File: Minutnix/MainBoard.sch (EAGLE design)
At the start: 142 parts, among them IC1 MEGA8-AI, IC10 TPIC6C596PW, IC11 TPIC6C596PW, IC12 TPIC6C596PW, IC13 TPIC6C596PW, IC2 TPIC6C596PW, IC3 TPIC6C596PW, IC4 TPIC6C596PW, IC5 TPIC6C596PW, IC6 TP4056, IC7 FT232RL, IC9 SC4503, Q4 32.768kHz, T1 DMN3024LSD, X1 FH12-12S-0.5SH, X2 87438-03, X3 87438-03

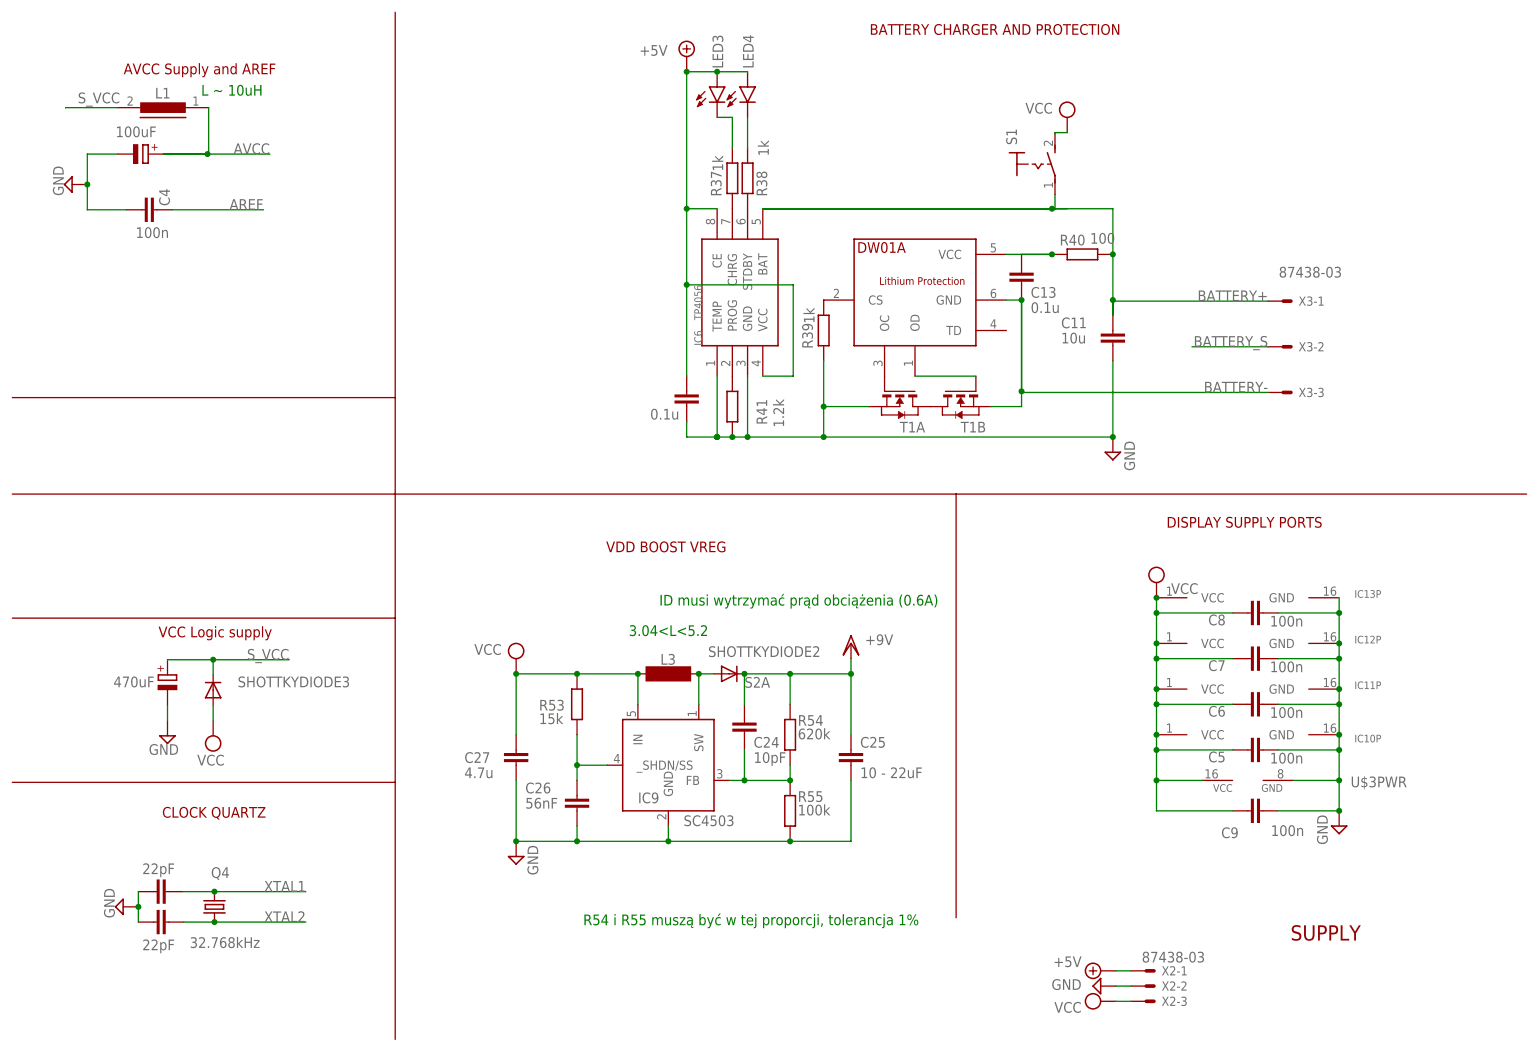
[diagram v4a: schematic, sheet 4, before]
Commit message: new lib + board progress
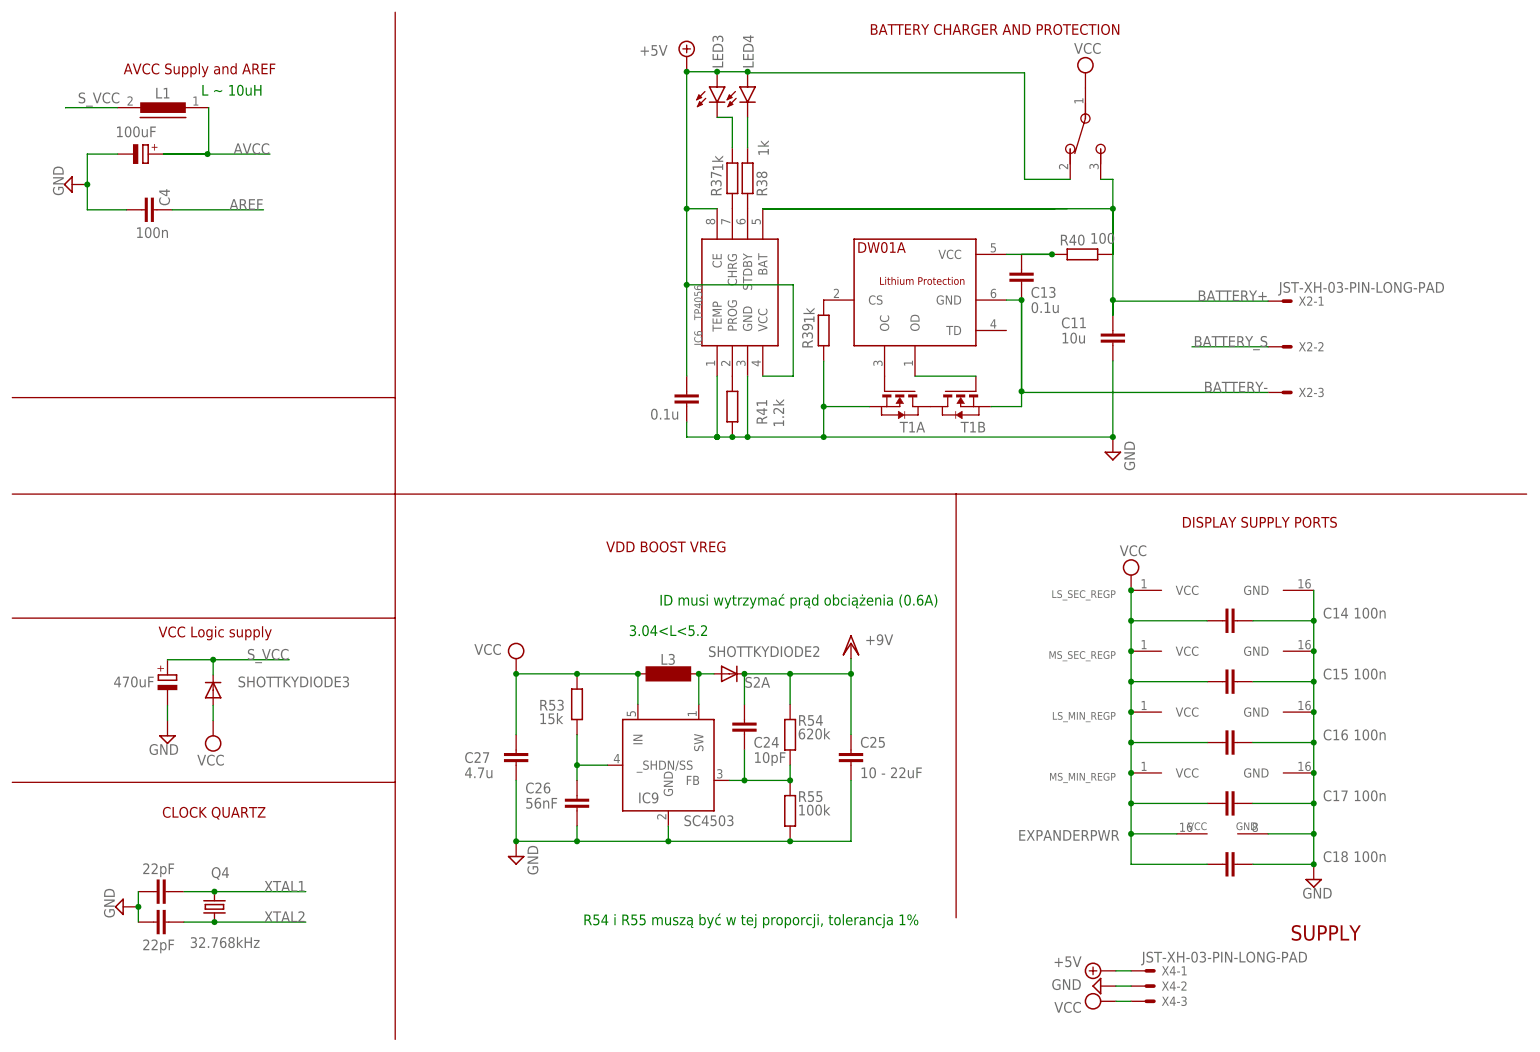
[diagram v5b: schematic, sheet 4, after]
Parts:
- removed C5, C6, C7, C8, C9: 100n, rcl:C-EUC0603
- removed IC10, IC11, IC12, IC13: TPIC6C596PW, tpic:TPIC6C596PW
- removed R35, R49: 100R, rcl:R-EU_R0603
- removed R48, R51, R59: 100, rcl:R-EU_R0603
- removed S1: (no value), switch:MS243
- removed U$3: PCF8574AT, i2c:PCF8574AT
- removed X3: 87438-03, con-molex:87438-03
- added C14, C15, C16, C17, C18: 100n, rcl:C-EUC0603
- added EXPANDER: PCF8574AT, i2c:PCF8574AT
- added X4: JST-XH-03-PIN-LONG-PAD, Rembrandt Electronics - JST XH Connectors v1-0:JST-XH-03-PIN-LONG-PAD
- LED3, LED4: device led:LED5MM -> led:LEDCHIPLED_0603
- R34, R50: value 100R -> 400R
- R47, R52, R64: value 100 -> 2k2
- R65, R66: value 100R -> 2k2
- U$1: value PCF8574AT -> SW; device i2c:PCF8574AT -> MySwitch:SW
- X2: value 87438-03 -> JST-XH-03-PIN-LONG-PAD; device con-molex:87438-03 -> Rembrandt Electronics - JST XH Connectors v1-0:JST-XH-03-PIN-LONG-PAD
- renumbered IC2 to LS_SEC_REG, IC3 to MS_SEC_REG, IC4 to LS_MIN_REG, IC5 to MS_MIN_REG, LSDIGIT to LSDIGIT_SECONDS, LSDIGIT1 to LSDIGIT_MINUTES, MSDIGIT to MSDIGIT_SECONDS, MSDIGIT1 to MSDIGIT_MINUTES
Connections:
- removed net N$29: R59.1, X1-8.1
- removed net N$49: R34.2, R35.1
- removed net N$52: R51.2, R64.1
- removed net N$53: R47.1, R48.2
- removed net N$54: R52.1, R59.2
- net +5V: now also U$1.2, X4-1.S; no longer X2-1.S
- net BATTERY+: now also U$1.3, X2-1.S; no longer S1.P, X3-1.S
- net BATTERY-: now also X2-3.S; no longer X3-3.S
- net BATTERY_S: now also X2-2.S; no longer X3-2.S
- net COUNTER: now also EXPANDERIC$1.P2, R44.2, X1-3.1; no longer R46.2, U$1IC$1.P0, X1-1.1
- net ENC_A: now also EXPANDERIC$1.P5; no longer U$1IC$1.P5
- net ENC_B: now also EXPANDERIC$1.P6; no longer U$1IC$1.P6
- net EXP_INT: now also EXPANDERIC$1./INT; no longer U$1IC$1./INT
- net EXP_SCL: now also EXPANDERIC$1.SCL; no longer U$1IC$1.SCL
- net EXP_SDA: now also EXPANDERIC$1.SDA; no longer U$1IC$1.SDA
- net GND: now also C14.1, C15.1, C16.1, C17.1, C18.1, EXPANDERIC$1.A0, EXPANDERIC$1.A1, EXPANDERIC$1.A2, EXPANDERPWR.GND, LS_MIN_REGP.GND, LS_SEC_REGP.GND, MS_MIN_REGP.GND, MS_SEC_REGP.GND, X4-2.S; no longer C5.2, C6.2, C7.2, C8.2, C9.2, IC10P.GND, IC11P.GND, IC12P.GND, IC13P.GND, U$1IC$1.A0, U$1IC$1.A1, U$1IC$1.A2, U$3PWR.GND, X2-2.S
- net N$12: now also R64.1, X1-10.1; no longer R49.1, R50.2
- net N$2: now also R50.2; no longer R49.2
- net N$20: now also R34.2; no longer R35.2
- net N$26: now also R47.1, X1-9.1; no longer R51.1, X1-10.1
- net N$28: now also R52.1, X1-8.1; no longer R48.1, X1-9.1
- net PLAY/PAUSE: now also EXPANDERIC$1.P1, R45.2, X1-2.1; no longer R43.2, U$1IC$1.P3, X1-4.1
- net STOP/RESET: now also EXPANDERIC$1.P0, R46.2, X1-1.1; no longer R42.2, U$1IC$1.P4, X1-5.1
- net UP1: now also EXPANDERIC$1.P7; no longer U$1IC$1.P7
- net VCC: now also C14.2, C15.2, C16.2, C17.2, C18.2, EXPANDERPWR.VCC, LS_MIN_REGP.VCC, LS_SEC_REGP.VCC, MS_MIN_REGP.VCC, MS_SEC_REGP.VCC, U$1.1, X4-3.S; no longer C5.1, C6.1, C7.1, C8.1, C9.1, IC10P.VCC, IC11P.VCC, IC12P.VCC, IC13P.VCC, S1.S, U$3PWR.VCC, X2-3.S
- net VOLUME: now also EXPANDERIC$1.P4, R42.2, X1-5.1; no longer R44.2, U$1IC$1.P2, X1-3.1
- net WARNING: now also EXPANDERIC$1.P3, R43.2, X1-4.1; no longer R45.2, U$1IC$1.P1, X1-2.1
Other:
- moved on the sheet: X2-1, X2-2, X2-3

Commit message: Resistor values updated
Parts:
- added R32, R35: 51R, rcl:R-EU_R0603
- PHOTORES: SPICEPREFIX (none) -> B
- R34, R50: value 400R -> 220R
- R37: value 1k -> 620R-1K
- R38: value 1k -> 620R-1k
- R47, R52, R64, R65, R66: value 2k2 -> 620R-1k
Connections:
- new net N$1: R32.2, R50.1
- new net N$49: R34.1, R35.2
- net N$50: now also R32.1; no longer R50.1
- net N$51: now also R35.1; no longer R34.1
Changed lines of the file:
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@@
 <part name="IC1" library="atmel" library_urn="urn:adsk.eagle:library:105" deviceset="MEGA8" device="-AI" package3d_urn="urn:adsk.eagle:package:4313/1"/>
 <part name="IC6" library="TP4056" deviceset="TP4056" device=""/>
-<part name="R37" library="rcl" library_urn="urn:adsk.eagle:library:334" deviceset="R-EU_" device="R1206" value="1k"/>
-<part name="R38" library="rcl" library_urn="urn:adsk.eagle:library:334" deviceset="R-EU_" device="R1206" value="1k"/>
+<part name="R37" library="rcl" library_urn="urn:adsk.eagle:library:334" deviceset="R-EU_" device="R1206" value="620R-1K"/>
+<part name="R38" library="rcl" library_urn="urn:adsk.eagle:library:334" deviceset="R-EU_" device="R1206" value="620R-1k"/>
 <part name="LED3" library="led" library_urn="urn:adsk.eagle:library:259" deviceset="LED" device="CHIPLED_0603" package3d_urn="urn:adsk.eagle:package:15822/2"/>
 <part name="LED4" library="led" library_urn="urn:adsk.eagle:library:259" deviceset="LED" device="CHIPLED_0603" package3d_urn="urn:adsk.eagle:package:15822/2"/>
@@
 <part name="SUPPLY23" library="supply2" library_urn="urn:adsk.eagle:library:372" deviceset="VCC" device=""/>
 <part name="VDD2" library="supply1" library_urn="urn:adsk.eagle:library:371" deviceset="VDD" device="" value="+9V"/>
-<part name="PHOTORES" library="photo-elements" library_urn="urn:adsk.eagle:library:323" deviceset="VT9" device="" package3d_urn="urn:adsk.eagle:package:22209/1" technology="0N1" value="VT90N1"/>
+<part name="PHOTORES" library="photo-elements" library_urn="urn:adsk.eagle:library:323" deviceset="VT9" device="" package3d_urn="urn:adsk.eagle:package:22209/1" technology="0N1" value="VT90N1">
+<attribute name="SPICEPREFIX" value="B"/>
+</part>
 <part name="SUPPLY21" library="supply2" library_urn="urn:adsk.eagle:library:372" deviceset="GND" device=""/>
 <part name="VDD4" library="supply1" library_urn="urn:adsk.eagle:library:371" deviceset="VDD" device="" value="+9V"/>
@@
 <part name="C3" library="rcl" library_urn="urn:adsk.eagle:library:334" deviceset="C-EU" device="C3216" package3d_urn="urn:adsk.eagle:package:23628/2" value="4.7u"/>
 <part name="SUPPLY33" library="supply2" library_urn="urn:adsk.eagle:library:372" deviceset="GND" device=""/>
-<part name="R66" library="rcl" library_urn="urn:adsk.eagle:library:334" deviceset="R-EU_" device="R0603" package3d_urn="urn:adsk.eagle:package:23555/2" value="2k2"/>
-<part name="R65" library="rcl" library_urn="urn:adsk.eagle:library:334" deviceset="R-EU_" device="R0603" package3d_urn="urn:adsk.eagle:package:23555/2" value="2k2"/>
+<part name="R66" library="rcl" library_urn="urn:adsk.eagle:library:334" deviceset="R-EU_" device="R0603" package3d_urn="urn:adsk.eagle:package:23555/2" value="620R-1k"/>
+<part name="R65" library="rcl" library_urn="urn:adsk.eagle:library:334" deviceset="R-EU_" device="R0603" package3d_urn="urn:adsk.eagle:package:23555/2" value="620R-1k"/>
 <part name="TXLED" library="led" library_urn="urn:adsk.eagle:library:259" deviceset="LED" device="CHIPLED_0603" package3d_urn="urn:adsk.eagle:package:15822/2"/>
 <part name="RXLED" library="led" library_urn="urn:adsk.eagle:library:259" deviceset="LED" device="CHIPLED_0603" package3d_urn="urn:adsk.eagle:package:15822/2"/>
@@
 <part name="R45" library="rcl" library_urn="urn:adsk.eagle:library:334" deviceset="R-EU_" device="R0603" package3d_urn="urn:adsk.eagle:package:23555/2" value="4.7k"/>
 <part name="R46" library="rcl" library_urn="urn:adsk.eagle:library:334" deviceset="R-EU_" device="R0603" package3d_urn="urn:adsk.eagle:package:23555/2" value="4.7k"/>
-<part name="R34" library="rcl" library_urn="urn:adsk.eagle:library:334" deviceset="R-EU_" device="R0603" package3d_urn="urn:adsk.eagle:package:23555/2" value="400R"/>
-<part name="R50" library="rcl" library_urn="urn:adsk.eagle:library:334" deviceset="R-EU_" device="R0603" package3d_urn="urn:adsk.eagle:package:23555/2" value="400R"/>
-<part name="R64" library="rcl" library_urn="urn:adsk.eagle:library:334" deviceset="R-EU_" device="R0603" package3d_urn="urn:adsk.eagle:package:23555/2" value="2k2"/>
-<part name="R47" library="rcl" library_urn="urn:adsk.eagle:library:334" deviceset="R-EU_" device="R0603" package3d_urn="urn:adsk.eagle:package:23555/2" value="2k2"/>
-<part name="R52" library="rcl" library_urn="urn:adsk.eagle:library:334" deviceset="R-EU_" device="R0603" package3d_urn="urn:adsk.eagle:package:23555/2" value="2k2"/>
+<part name="R50" library="rcl" library_urn="urn:adsk.eagle:library:334" deviceset="R-EU_" device="R0603" package3d_urn="urn:adsk.eagle:package:23555/2" value="220R"/>
+<part name="R64" library="rcl" library_urn="urn:adsk.eagle:library:334" deviceset="R-EU_" device="R0603" package3d_urn="urn:adsk.eagle:package:23555/2" value="620R-1k"/>
+<part name="R47" library="rcl" library_urn="urn:adsk.eagle:library:334" deviceset="R-EU_" device="R0603" package3d_urn="urn:adsk.eagle:package:23555/2" value="620R-1k"/>
+<part name="R52" library="rcl" library_urn="urn:adsk.eagle:library:334" deviceset="R-EU_" device="R0603" package3d_urn="urn:adsk.eagle:package:23555/2" value="620R-1k"/>
 <part name="GND1" library="supply1" library_urn="urn:adsk.eagle:library:371" deviceset="GNDA" device=""/>
 <part name="GND2" library="supply1" library_urn="urn:adsk.eagle:library:371" deviceset="GNDA" device=""/>
@@
 <part name="U$1" library="MySwitch" deviceset="SW" device=""/>
 <part name="SUPPLY6" library="supply2" library_urn="urn:adsk.eagle:library:372" deviceset="VCC" device=""/>
+<part name="R32" library="rcl" library_urn="urn:adsk.eagle:library:334" deviceset="R-EU_" device="R0603" package3d_urn="urn:adsk.eagle:package:23555/2" value="51R"/>
+<part name="R34" library="rcl" library_urn="urn:adsk.eagle:library:334" deviceset="R-EU_" device="R0603" package3d_urn="urn:adsk.eagle:package:23555/2" value="220R"/>
+<part name="R35" library="rcl" library_urn="urn:adsk.eagle:library:334" deviceset="R-EU_" device="R0603" package3d_urn="urn:adsk.eagle:package:23555/2" value="51R"/>
 </parts>
 <sheets>
@@
 <instance part="R20" gate="G$1" x="150.16" y="144.58" smashed="yes" rot="R180"/>
 <instance part="R21" gate="G$1" x="150.16" y="147.12" smashed="yes" rot="R180"/>
+<instance part="R50" gate="G$1" x="145.08" y="98.86" smashed="yes" rot="R180">
+<attribute name="VALUE" x="148.89" y="102.162" size="1.778" layer="96" rot="R180"/>
+</instance>
+<instance part="R32" gate="G$1" x="155.24" y="98.86" smashed="yes" rot="R180">
+<attribute name="VALUE" x="159.05" y="102.162" size="1.778" layer="96" rot="R180"/>
+</instance>
 <instance part="R34" gate="G$1" x="145.08" y="70.92" smashed="yes" rot="R180">
 <attribute name="VALUE" x="148.89" y="74.222" size="1.778" layer="96" rot="R180"/>
 </instance>
-<instance part="R50" gate="G$1" x="145.08" y="98.86" smashed="yes" rot="R180">
-<attribute name="VALUE" x="148.89" y="102.162" size="1.778" layer="96" rot="R180"/>
+<instance part="R35" gate="G$1" x="155.24" y="70.92" smashed="yes" rot="R180">
+<attribute name="VALUE" x="159.05" y="74.222" size="1.778" layer="96" rot="R180"/>
 </instance>
 </instances>
@@
 <net name="N$50" class="0">
 <segment>
-<pinref part="R50" gate="G$1" pin="1"/>
 <pinref part="COLON1" gate="G$1" pin="C"/>
-<wire x1="150.16" y1="98.86" x2="162.86" y2="98.86" width="0.1524" layer="91"/>
-</segment>
-</net>
-<net name="N$51" class="0">
-<segment>
-<pinref part="R34" gate="G$1" pin="1"/>
-<pinref part="COLON2" gate="G$1" pin="C"/>
-<wire x1="150.16" y1="70.92" x2="162.86" y2="70.92" width="0.1524" layer="91"/>
+<wire x1="160.32" y1="98.86" x2="162.86" y2="98.86" width="0.1524" layer="91"/>
+<pinref part="R32" gate="G$1" pin="1"/>
 </segment>
 </net>
@@
 <wire x1="140" y1="101.4" x2="127.3" y2="101.4" width="0.1524" layer="91"/>
 <pinref part="R50" gate="G$1" pin="2"/>
+</segment>
+</net>
+<net name="N$1" class="0">
+<segment>
+<pinref part="R50" gate="G$1" pin="1"/>
+<pinref part="R32" gate="G$1" pin="2"/>
+</segment>
+</net>
+<net name="N$49" class="0">
+<segment>
+<pinref part="R34" gate="G$1" pin="1"/>
+<pinref part="R35" gate="G$1" pin="2"/>
+</segment>
+</net>
+<net name="N$51" class="0">
+<segment>
+<pinref part="R35" gate="G$1" pin="1"/>
+<pinref part="COLON2" gate="G$1" pin="C"/>
+<wire x1="160.32" y1="70.92" x2="162.86" y2="70.92" width="0.1524" layer="91"/>
 </segment>
 </net>
@@
 <instance part="R37" gate="G$1" x="123.96" y="147.5" smashed="yes" rot="R90">
 <attribute name="NAME" x="120.3786" y="148.77" size="1.778" layer="95" rot="R270"/>
-<attribute name="VALUE" x="120.658" y="151.31" size="1.778" layer="96" rot="R270"/>
 </instance>
 <instance part="R38" gate="G$1" x="126.5" y="147.5" smashed="yes" rot="R90">
 <attribute name="NAME" x="127.9986" y="148.77" size="1.778" layer="95" rot="R270"/>
-<attribute name="VALUE" x="128.278" y="153.85" size="1.778" layer="96" rot="R270"/>
+<attribute name="VALUE" x="130.818" y="153.85" size="1.778" layer="96" rot="R270"/>
 </instance>
 <instance part="LED3" gate="G$1" x="121.42" y="162.74" smashed="yes">
